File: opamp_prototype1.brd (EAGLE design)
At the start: 51.1 x 39.4 mm, 18 parts, among them IC1 OPA2132P, IC2 OPA2132U

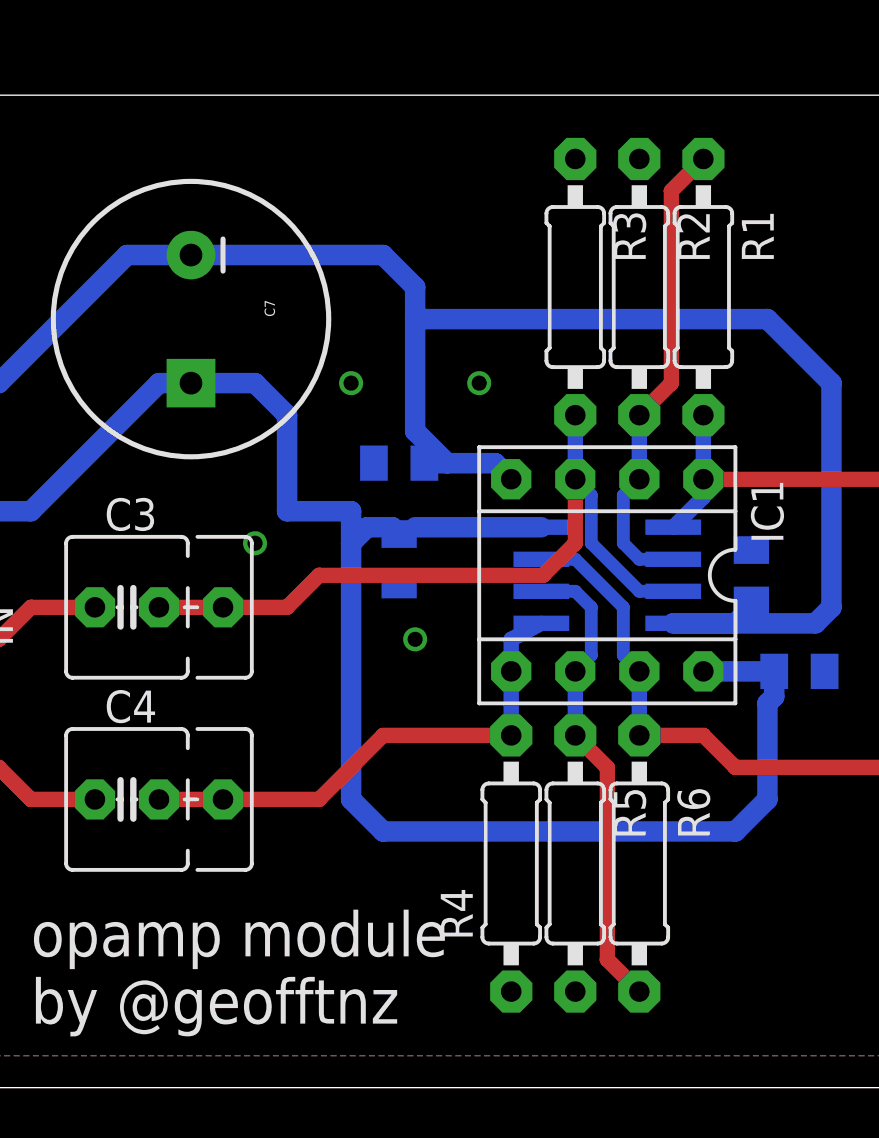
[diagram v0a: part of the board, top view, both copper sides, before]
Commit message: Added SMD resistor option
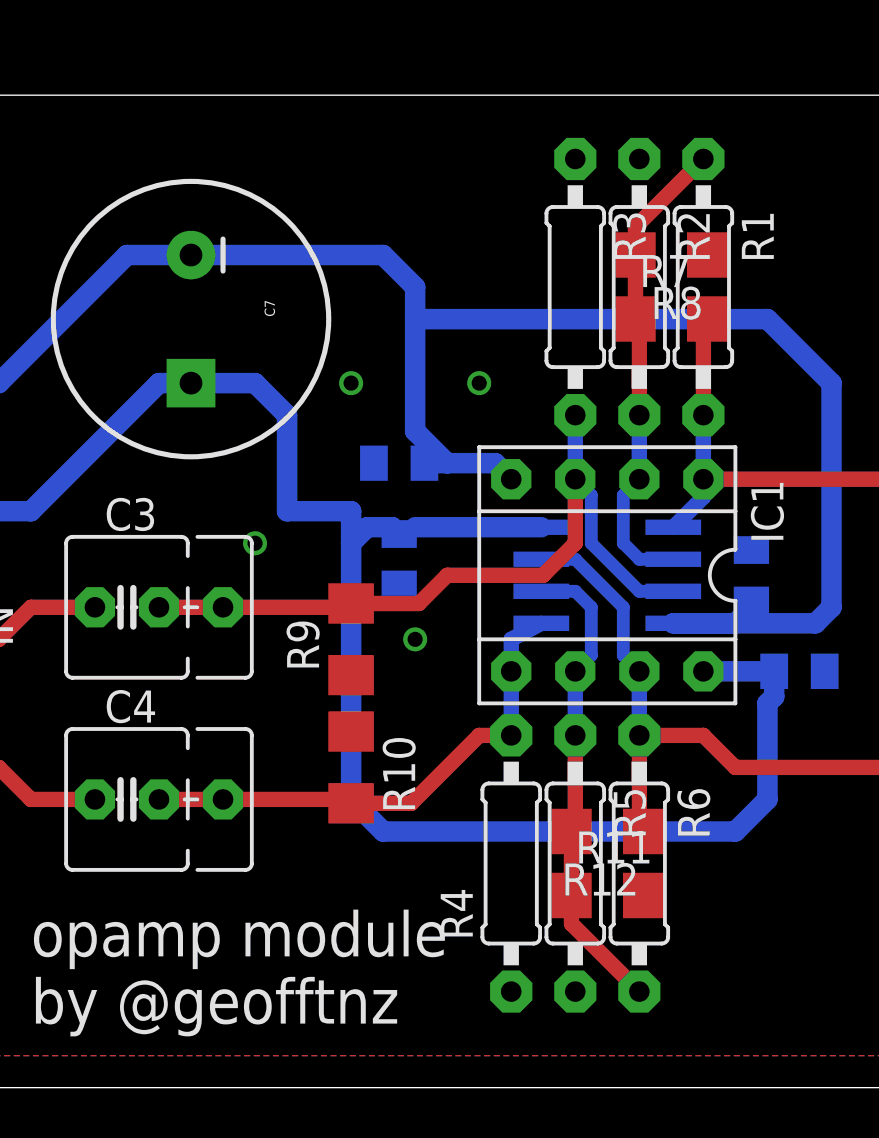
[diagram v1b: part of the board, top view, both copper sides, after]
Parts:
- added R10, R11, R12, R7, R8, R9: (no value), rcl:R1206
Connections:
- net GND: now also R10.1, R11.2, R8.1, R9.1
- net LAMP+: now also R9.2
- net LAMP-: now also R7.1, R8.2
- net OUT_L: now also R7.2
- net OUT_R: now also R12.1
- net RAMP+: now also R10.2
- net RAMP-: now also R11.1, R12.2
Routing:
- net OUT_L: track 21.2 -> 25.1 mm
- net OUT_R: track 23.9 -> 27.8 mm
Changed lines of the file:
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@@
 <layers>
 <layer number="1" name="Top" color="4" fill="1" visible="yes" active="yes"/>
-<layer number="16" name="Bottom" color="1" fill="1" visible="yes" active="yes"/>
+<layer number="16" name="Bottom" color="1" fill="1" visible="no" active="yes"/>
 <layer number="17" name="Pads" color="2" fill="1" visible="yes" active="yes"/>
 <layer number="18" name="Vias" color="2" fill="1" visible="yes" active="yes"/>
@@
 <dimension x1="0" y1="0" x2="51.105" y2="0" x3="25.5525" y3="-3.81" textsize="1.778" layer="48"/>
 <dimension x1="51.105" y1="39.36" x2="51.105" y2="0" x3="57.15" y3="19.68" textsize="1.778" layer="48"/>
+<rectangle x1="33.9725" y1="30.7975" x2="34.925" y2="35.2425" layer="41"/>
+<rectangle x1="31.115" y1="5.715" x2="32.385" y2="9.525" layer="41"/>
 </plain>
 <attributes>
@@
 <element name="IN" library="SparkFun-Connectors" package="1X03" value="" x="5.08" y="17.78" rot="R270"/>
 <element name="OUT" library="SparkFun-Connectors" package="1X03" value="" x="46.99" y="17.78" rot="R270"/>
+<element name="R7" library="rcl" package="R1206" value="" x="34.29" y="30.48"/>
+<element name="R8" library="rcl" package="R1206" value="" x="34.29" y="33.02" rot="R180"/>
+<element name="R9" library="rcl" package="R1206" value="" x="21.59" y="17.78" rot="R90"/>
+<element name="R10" library="rcl" package="R1206" value="" x="21.59" y="12.7" rot="R270"/>
+<element name="R11" library="rcl" package="R1206" value="" x="31.75" y="7.62"/>
+<element name="R12" library="rcl" package="R1206" value="" x="31.75" y="10.16" rot="R180"/>
 </elements>
 <signals>
@@
 <via x="21.59" y="27.94" extent="1-16" drill="0.6" shape="square"/>
 <via x="26.67" y="27.94" extent="1-16" drill="0.6" shape="square"/>
+<contactref element="R9" pad="1"/>
+<contactref element="R10" pad="1"/>
+<contactref element="R11" pad="2"/>
+<contactref element="R8" pad="1"/>
 </signal>
 <signal name="LAMP+">
@@
 <wire x1="30.48" y1="24.13" x2="30.48" y2="21.59" width="0.6096" layer="1"/>
 <wire x1="30.48" y1="21.59" x2="29.21" y2="20.32" width="0.6096" layer="1"/>
-<wire x1="29.21" y1="20.32" x2="20.32" y2="20.32" width="0.6096" layer="1"/>
-<wire x1="20.32" y1="20.32" x2="19.05" y2="19.05" width="0.6096" layer="1"/>
-<wire x1="19.05" y1="19.05" x2="13.97" y2="19.05" width="0.6096" layer="1"/>
+<contactref element="R9" pad="2"/>
+<wire x1="13.97" y1="19.05" x2="21.438" y2="19.05" width="0.6096" layer="1"/>
+<wire x1="21.438" y1="19.05" x2="21.59" y2="19.202" width="0.6096" layer="1"/>
+<wire x1="21.59" y1="19.202" x2="24.282" y2="19.202" width="0.6096" layer="1"/>
+<wire x1="24.282" y1="19.202" x2="25.4" y2="20.32" width="0.6096" layer="1"/>
+<wire x1="25.4" y1="20.32" x2="29.21" y2="20.32" width="0.6096" layer="1"/>
 </signal>
 <signal name="RAMP+">
@@
 <wire x1="27.94" y1="17.78" x2="29.1338" y2="18.415" width="0.6096" layer="16"/>
 <wire x1="27.94" y1="16.51" x2="27.94" y2="13.97" width="0.6096" layer="16"/>
-<wire x1="13.97" y1="11.43" x2="20.32" y2="11.43" width="0.6096" layer="1"/>
-<wire x1="20.32" y1="11.43" x2="22.86" y2="13.97" width="0.6096" layer="1"/>
-<wire x1="22.86" y1="13.97" x2="27.94" y2="13.97" width="0.6096" layer="1"/>
+<contactref element="R10" pad="2"/>
+<wire x1="13.97" y1="11.43" x2="21.438" y2="11.43" width="0.6096" layer="1"/>
+<wire x1="21.438" y1="11.43" x2="21.59" y2="11.278" width="0.6096" layer="1"/>
+<wire x1="21.59" y1="11.278" x2="23.978" y2="11.278" width="0.6096" layer="1"/>
+<wire x1="23.978" y1="11.278" x2="26.67" y2="13.97" width="0.6096" layer="1"/>
+<wire x1="26.67" y1="13.97" x2="27.94" y2="13.97" width="0.6096" layer="1"/>
 </signal>
 <signal name="OUT_R">
@@
 <wire x1="35.56" y1="13.97" x2="36.83" y2="12.7" width="0.6096" layer="1"/>
 <wire x1="36.83" y1="12.7" x2="46.99" y2="12.7" width="0.6096" layer="1"/>
+<contactref element="R12" pad="1"/>
+<wire x1="33.02" y1="13.97" x2="33.02" y2="10.312" width="0.6096" layer="1"/>
+<wire x1="33.02" y1="10.312" x2="33.172" y2="10.16" width="0.6096" layer="1"/>
 </signal>
 <signal name="RAMP-">
@@
 <wire x1="30.48" y1="19.685" x2="29.1338" y2="19.685" width="0.508" layer="16"/>
 <wire x1="30.48" y1="16.51" x2="30.48" y2="13.97" width="0.6096" layer="16"/>
-<wire x1="33.02" y1="3.81" x2="31.75" y2="5.08" width="0.6096" layer="1"/>
-<wire x1="31.75" y1="5.08" x2="31.75" y2="12.7" width="0.6096" layer="1"/>
-<wire x1="31.75" y1="12.7" x2="30.48" y2="13.97" width="0.6096" layer="1"/>
+<contactref element="R11" pad="1"/>
+<contactref element="R12" pad="2"/>
+<wire x1="30.48" y1="13.97" x2="30.48" y2="10.312" width="0.6096" layer="1"/>
+<wire x1="30.48" y1="10.312" x2="30.328" y2="10.16" width="0.6096" layer="1"/>
+<wire x1="30.328" y1="10.16" x2="30.328" y2="7.62" width="0.6096" layer="1"/>
+<wire x1="30.328" y1="7.62" x2="30.328" y2="6.502" width="0.6096" layer="1"/>
+<wire x1="30.328" y1="6.502" x2="33.02" y2="3.81" width="0.6096" layer="1"/>
 </signal>
 <signal name="OUT_L">
@@
 <wire x1="35.56" y1="24.13" x2="35.56" y2="23.4188" width="0.6096" layer="16"/>
 <wire x1="35.56" y1="23.4188" x2="34.3662" y2="22.225" width="0.6096" layer="16"/>
+<contactref element="R7" pad="2"/>
+<wire x1="35.56" y1="26.67" x2="35.56" y2="30.328" width="0.6096" layer="1"/>
+<wire x1="35.56" y1="30.328" x2="35.712" y2="30.48" width="0.6096" layer="1"/>
 </signal>
 <signal name="LAMP-">
@@
 <wire x1="33.02" y1="20.955" x2="34.3662" y2="20.955" width="0.508" layer="16"/>
 <wire x1="33.02" y1="24.13" x2="33.02" y2="26.67" width="0.6096" layer="16"/>
-<wire x1="33.02" y1="26.67" x2="34.29" y2="27.94" width="0.6096" layer="1"/>
-<wire x1="34.29" y1="27.94" x2="34.29" y2="35.56" width="0.6096" layer="1"/>
-<wire x1="34.29" y1="35.56" x2="35.56" y2="36.83" width="0.6096" layer="1"/>
+<contactref element="R7" pad="1"/>
+<contactref element="R8" pad="2"/>
+<wire x1="33.02" y1="26.67" x2="33.02" y2="30.328" width="0.6096" layer="1"/>
+<wire x1="33.02" y1="30.328" x2="32.868" y2="30.48" width="0.6096" layer="1"/>
+<wire x1="32.868" y1="30.48" x2="32.868" y2="33.02" width="0.6096" layer="1"/>
+<wire x1="32.868" y1="33.02" x2="32.868" y2="34.138" width="0.6096" layer="1"/>
+<wire x1="32.868" y1="34.138" x2="35.56" y2="36.83" width="0.6096" layer="1"/>
 </signal>
 <signal name="IN_L">

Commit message: tidy up
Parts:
- moved R10 6.48 mm to (20.3, 6.35)
- moved C3 6.35 mm to (12.7, 12.7)
- moved R9 5.24 mm to (20.3, 12.7)
- moved C4 5.08 mm to (12.7, 6.35)
- moved IN 2.54 mm to (5.08, 15.2)
- moved C1 1.27 mm to (23.5, 22.2), turned to 0 degrees
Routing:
- net RAMP+: track 20.3 -> 27.2 mm
- net LAMP+: track 29.5 -> 34.1 mm
- net V+: track 67.9 -> 65.9 mm
- net N$3: track 6.88 -> 7.93 mm
- net IN_L: track 6.88 -> 7.40 mm
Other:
- board size 51.1 x 39.4 mm -> 49.5 x 39.4 mm
